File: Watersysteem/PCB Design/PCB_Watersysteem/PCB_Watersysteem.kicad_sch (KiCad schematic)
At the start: 54 parts, among them J1 Screw_Terminal_01x02, J10 LED Water Level, J11 LED Nutrient Level, J12 Height Nutrients, J13 Height Mixer, J2 Conn_01x04_Pin, J21 Voedingstoffen 1, J3 ReferentieProbe, J4 Voedingstoffen 2, J5 Voedingstoffen 3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

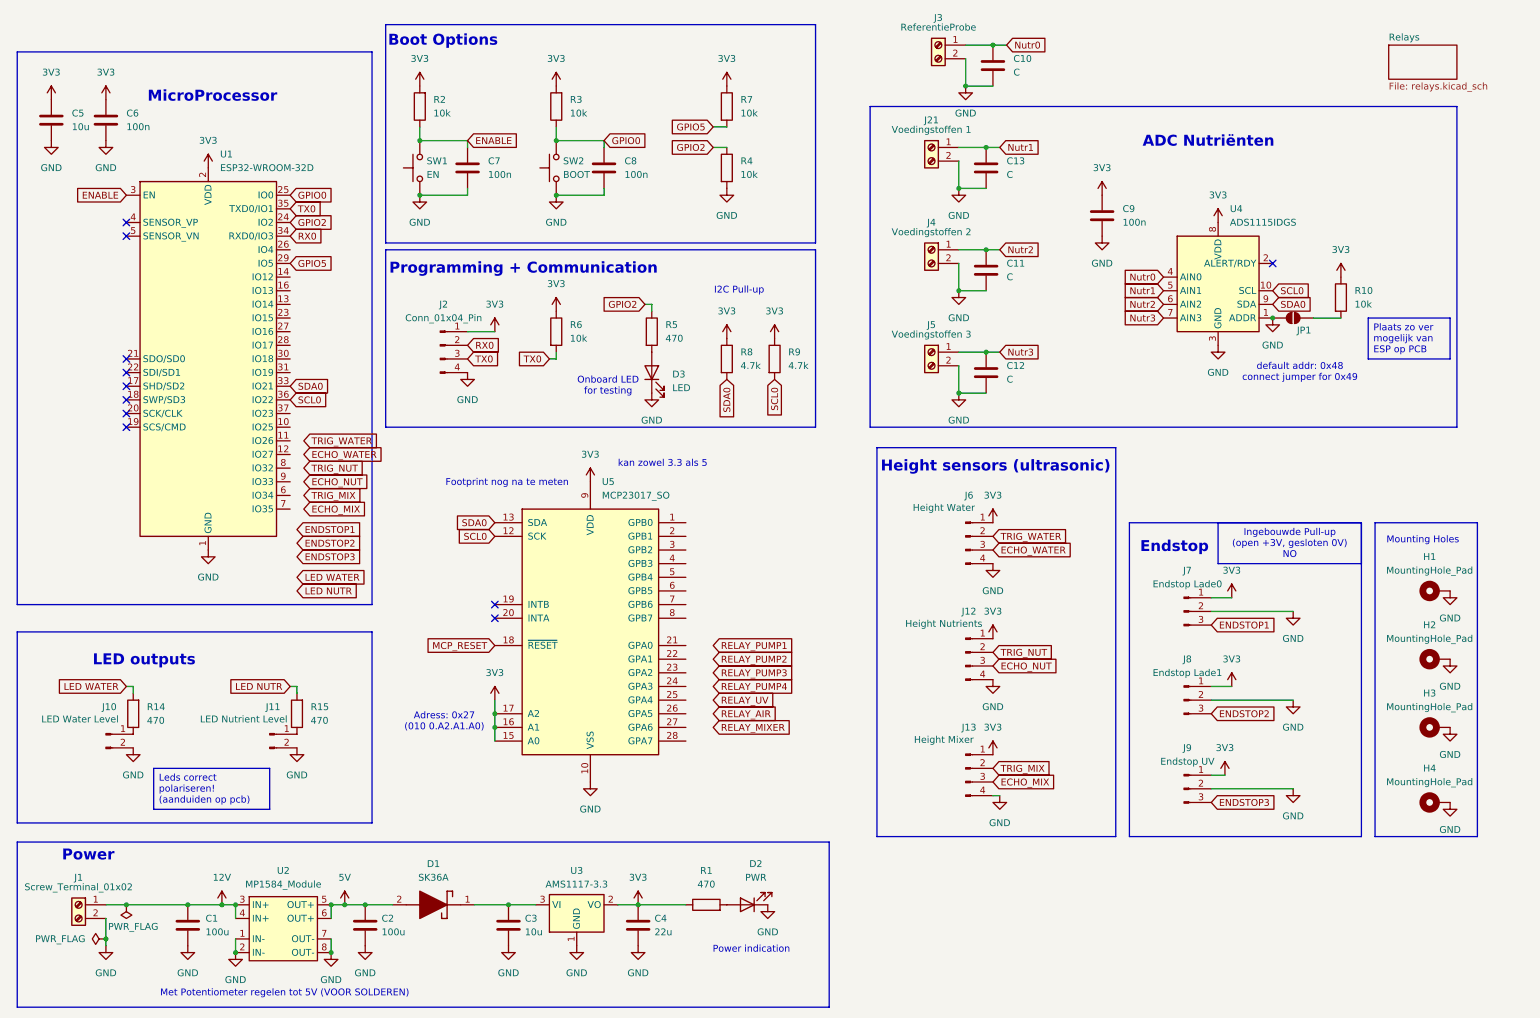
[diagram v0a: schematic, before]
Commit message: PCB update
Testpunten, relaisschakelingen afgewerkt, adres io expander wijzigbaar, enkele footprints
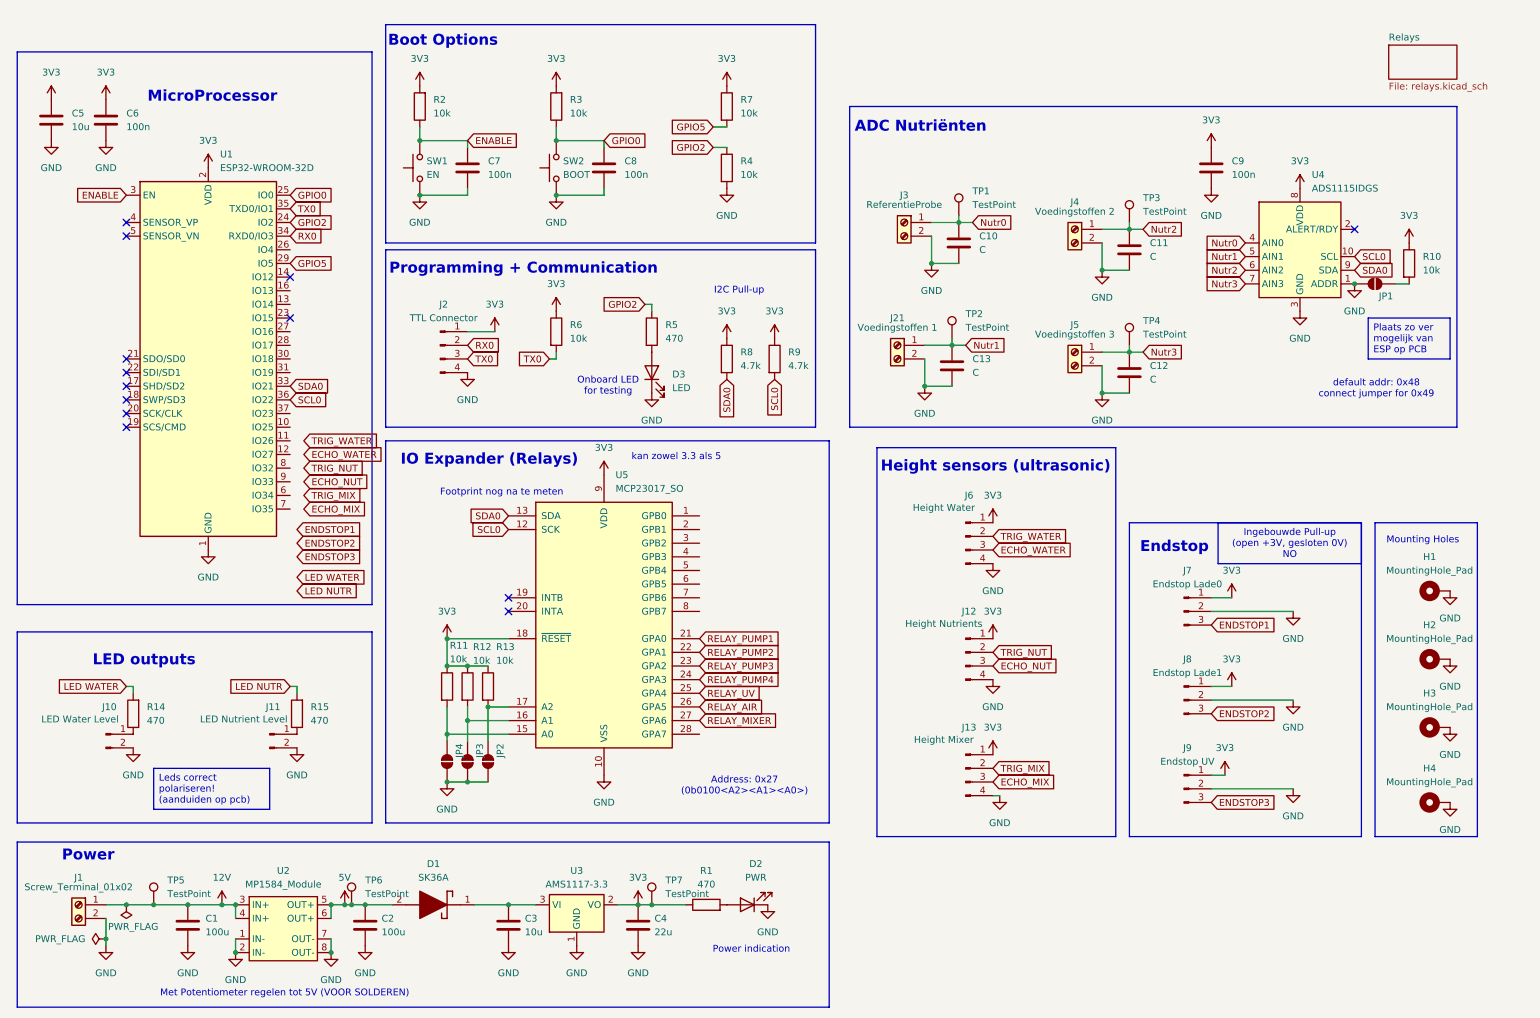
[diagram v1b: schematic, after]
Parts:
- added JP2, JP3, JP4: SolderJumper_2_Open, Jumper:SolderJumper-2_P1.3mm_Open_RoundedPad1.0x1.5mm, symbol Jumper:SolderJumper_2_Open
- added R11, R12, R13: 10k, Resistor_SMD:R_0805_2012Metric_Pad1.20x1.40mm_HandSolder, symbol Device:R
- added TP1, TP2, TP3, TP4, TP5, TP6, TP7: TestPoint, TestPoint:TestPoint_Pad_D2.5mm, symbol Connector:TestPoint
- J10, J11: footprint (none) -> Connector_PinHeader_2.54mm:PinHeader_1x02_P2.54mm_Vertical
- J12, J13, J6: footprint (none) -> Connector_PinHeader_2.54mm:PinHeader_1x04_P2.54mm_Vertical
- J2: value Conn_01x04_Pin -> TTL Connector; footprint (none) -> Connector_PinHeader_2.54mm:PinHeader_1x04_P2.54mm_Vertical
- J7, J8, J9: footprint (none) -> Connector_PinHeader_2.54mm:PinHeader_1x03_P2.54mm_Vertical
- JP1: footprint (none) -> Jumper:SolderJumper-2_P1.3mm_Open_RoundedPad1.0x1.5mm
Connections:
- net MCP_RESET is gone; now on net 3V3: U5.18 (~{RESET})
- net 12V: now also TP5.1
- net 3V3: now also R11.1, R12.1, R13.1, TP7.1; no longer U5.15 (A0), U5.16 (A1), U5.17 (A2)
- net 5V: now also TP6.1
- net GND: now also JP2.1 (A), JP3.1 (A), JP4.1 (A)
- net Nutr0: now also TP1.1
- net Nutr1: now also TP2.1
- net Nutr2: now also TP3.1
- net Nutr3: now also TP4.1
- net RELAY_AIR: now also U5.26 (GPA5)
- net RELAY_MIXER: now also U5.27 (GPA6)
- net RELAY_PUMP1: now also U5.21 (GPA0)
- net RELAY_PUMP2: now also U5.22 (GPA1)
- net RELAY_PUMP3: now also U5.23 (GPA2)
- net RELAY_PUMP4: now also U5.24 (GPA3)
- net RELAY_UV: now also U5.25 (GPA4)
- new net: JP4.2 (B), R11.2, U5.15 (A0)
- new net: JP3.2 (B), R12.2, U5.16 (A1)
- new net: JP2.2 (B), R13.2, U5.17 (A2)
- no-connect marks 11 -> 13
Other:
- note added: "Address: 0x27 (0b0100<A2><A1><A0>)"
- note added: "IO Expander (Relays)"
- note removed: "Adress: 0x27 (010 0.A2.A1.A0)"
- moved on the sheet: C10, C11, C12, C13, C9, J21, J3, J4, J5, JP1, R10, U4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

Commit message: Update PCB
Switch library toegevoegd, IO expander ontkoppel toegevoegd
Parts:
- added C14: 100n, symbol Device:C
- SW1, SW2: footprint (none) -> SamacSys_Parts:Wurth_Tactile_Switch_SPST-NO_434111043826
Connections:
- net 3V3: now also C14.1
- net GND: now also C14.2
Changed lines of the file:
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@@
 			)
 		)
-		(property "Footprint" ""
+		(property "Footprint" "SamacSys_Parts:Wurth_Tactile_Switch_SPST-NO_434111043826"
 			(at 107.95 40.64 0)
 			(effects
@@
 	)
 	(symbol
+		(lib_id "power:VCC")
+		(at 149.86 99.06 0)
+		(unit 1)
+		(exclude_from_sim no)
+		(in_bom yes)
+		(on_board yes)
+		(dnp no)
+		(fields_autoplaced yes)
+		(property "Reference" "#PWR089"
+			(at 149.86 102.87 0)
+			(effects
+				(font
+					(size 1.27 1.27)
+				)
+				(hide yes)
+			)
+		)
+		(property "Value" "3V3"
+			(at 149.86 93.98 0)
+			(effects
+				(font
+					(size 1.27 1.27)
+				)
+			)
+		)
+		(property "Footprint" ""
+			(at 149.86 99.06 0)
+			(effects
+				(font
+					(size 1.27 1.27)
+				)
+				(hide yes)
+			)
+		)
+		(property "Datasheet" ""
+			(at 149.86 99.06 0)
+			(effects
+				(font
+					(size 1.27 1.27)
+				)
+				(hide yes)
+			)
+		)
+		(property "Description" "Power symbol creates a global label with name \"VCC\""
+			(at 149.86 99.06 0)
+			(effects
+				(font
+					(size 1.27 1.27)
+				)
+				(hide yes)
+			)
+		)
+		(pin "1"
+		)
+		(instances
+			(project "PCB_Watersysteem"
+				(path "/de0b8b90-8fde-4ab1-b1b1-e85d44454ecd"
+					(reference "#PWR089")
+					(unit 1)
+				)
+			)
+		)
+	)
+	(symbol
 		(lib_id "Mechanical:MountingHole_Pad")
 		(at 276.86 144.78 90)
@@
 			)
 		)
-		(property "Footprint" ""
+		(property "Footprint" "SamacSys_Parts:Wurth_Tactile_Switch_SPST-NO_434111043826"
 			(at 82.55 40.64 0)
 			(effects
@@
 	(symbol
 		(lib_id "power:GND")
+		(at 149.86 106.68 0)
+		(unit 1)
+		(exclude_from_sim no)
+		(in_bom yes)
+		(on_board yes)
+		(dnp no)
+		(fields_autoplaced yes)
+		(property "Reference" "#PWR088"
+			(at 149.86 113.03 0)
+			(effects
+				(font
+					(size 1.27 1.27)
+				)
+				(hide yes)
+			)
+		)
+		(property "Value" "GND"
+			(at 149.86 111.76 0)
+			(effects
+				(font
+					(size 1.27 1.27)
+				)
+			)
+		)
+		(property "Footprint" ""
+			(at 149.86 106.68 0)
+			(effects
+				(font
+					(size 1.27 1.27)
+				)
+				(hide yes)
+			)
+		)
+		(property "Datasheet" ""
+			(at 149.86 106.68 0)
+			(effects
+				(font
+					(size 1.27 1.27)
+				)
+				(hide yes)
+			)
+		)
+		(property "Description" "Power symbol creates a global label with name \"GND\" , ground"
+			(at 149.86 106.68 0)
+			(effects
+				(font
+					(size 1.27 1.27)
+				)
+				(hide yes)
+			)
+		)
+		(pin "1"
+		)
+		(instances
+			(project "PCB_Watersysteem"
+				(path "/de0b8b90-8fde-4ab1-b1b1-e85d44454ecd"
+					(reference "#PWR088")
+					(unit 1)
+				)
+			)
+		)
+	)
+	(symbol
+		(lib_id "power:GND")
 		(at 92.71 154.94 0)
 		(unit 1)
@@
 					(unit 1)
 				)
+			)
+		)
+	)
+	(symbol
+		(lib_id "Device:C")
+		(at 149.86 102.87 0)
+		(unit 1)
+		(exclude_from_sim no)
+		(in_bom yes)
+		(on_board yes)
+		(dnp no)
+		(fields_autoplaced yes)
+		(property "Reference" "C14"
+			(at 153.67 101.5999 0)
+			(effects
+				(font
+					(size 1.27 1.27)
+				)
+				(justify left)
+			)
+		)
+		(property "Value" "100n"
+			(at 153.67 104.1399 0)
+			(effects
+				(font
+					(size 1.27 1.27)
+				)
+				(justify left)
+			)
+		)
+		(property "Footprint" ""
+			(at 150.8252 106.68 0)
+			(effects
+				(font
+					(size 1.27 1.27)
+				)
+				(hide yes)
+			)
+		)
+		(property "Datasheet" "~"
+			(at 149.86 102.87 0)
+			(effects
+				(font
+					(size 1.27 1.27)
+				)
+				(hide yes)
+			)
+		)
+		(property "Description" "Unpolarized capacitor"
+			(at 149.86 102.87 0)
+			(effects
+				(font
+					(size 1.27 1.27)
+				)
+				(hide yes)
+			)
+		)
+		(pin "2"
+		)
+		(pin "1"
+		)
+		(instances
+			(project ""
+				(path "/de0b8b90-8fde-4ab1-b1b1-e85d44454ecd"
+					(reference "C14")
+					(unit 1)
+				)

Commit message: Update PCB
Footprints toegevoegd
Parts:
- H1, H2, H3, H4: footprint (none) -> MountingHole:MountingHole_4.3mm_M4_DIN965_Pad_TopBottom
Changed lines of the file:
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@@
 			)
 		)
-		(property "Footprint" ""
+		(property "Footprint" "MountingHole:MountingHole_4.3mm_M4_DIN965_Pad_TopBottom"
 			(at 276.86 144.78 0)
 			(effects
@@
 			)
 		)
-		(property "Footprint" ""
+		(property "Footprint" "MountingHole:MountingHole_4.3mm_M4_DIN965_Pad_TopBottom"
 			(at 276.86 158.75 0)
 			(effects
@@
 			)
 		)
-		(property "Footprint" ""
+		(property "Footprint" "MountingHole:MountingHole_4.3mm_M4_DIN965_Pad_TopBottom"
 			(at 276.86 132.08 0)
 			(effects
@@
 			)
 		)
-		(property "Footprint" ""
+		(property "Footprint" "MountingHole:MountingHole_4.3mm_M4_DIN965_Pad_TopBottom"
 			(at 276.86 119.38 0)
 			(effects

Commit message: Update PCB
IO gemapt, Condensator ADC, Schematic geprint
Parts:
- added TP15: TestPoint, TestPoint:TestPoint_Pad_D2.5mm, symbol Connector:TestPoint
- C10, C11, C12, C13: value C -> 100n; footprint (none) -> Capacitor_SMD:C_0805_2012Metric_Pad1.18x1.45mm_HandSolder
- C14: footprint (none) -> Capacitor_SMD:C_0805_2012Metric_Pad1.18x1.45mm_HandSolder
- J1: value Screw_Terminal_01x02 -> 12V ingang
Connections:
- net ECHO_MIX: now also U1.13 (IO14)
- net ECHO_NUT: now also U1.11 (IO26)
- net ECHO_WATER: now also U1.9 (IO33)
- net ENDSTOP1: now also U1.28 (IO17)
- net ENDSTOP2: now also U1.27 (IO16)
- net ENDSTOP3: now also U1.26 (IO4)
- net GND: now also TP15.1
- net LED NUTR: now also U1.31 (IO19)
- net LED WATER: now also U1.30 (IO18)
- net TRIG_MIX: now also U1.12 (IO27)
- net TRIG_NUT: now also U1.10 (IO25)
- net TRIG_WATER: now also U1.8 (IO32)
- no-connect marks 13 -> 26
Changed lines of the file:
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@@
 	)
 	(no_connect
+		(at 139.7 115.57)
+	)
+	(no_connect
 		(at 104.14 123.19)
 	)
@@
 	)
 	(no_connect
+		(at 139.7 113.03)
+	)
+	(no_connect
+		(at 139.7 107.95)
+	)
+	(no_connect
+		(at 139.7 105.41)
+	)
+	(no_connect
+		(at 139.7 146.05)
+	)
+	(no_connect
 		(at 63.5 68.58)
 	)
 	(no_connect
+		(at 139.7 110.49)
+	)
+	(no_connect
 		(at 261.62 52.07)
 	)
 	(no_connect
+		(at 63.5 63.5)
+	)
+	(no_connect
 		(at 33.02 86.36)
 	)
@@
 	)
 	(no_connect
+		(at 63.5 101.6)
+	)
+	(no_connect
+		(at 63.5 104.14)
+	)
+	(no_connect
+		(at 139.7 123.19)
+	)
+	(no_connect
 		(at 104.14 120.65)
 	)
 	(no_connect
+		(at 63.5 86.36)
+	)
+	(no_connect
 		(at 33.02 78.74)
 	)
 	(no_connect
+		(at 139.7 120.65)
+	)
+	(no_connect
 		(at 33.02 50.8)
 	)
 	(no_connect
+		(at 139.7 118.11)
+	)
+	(no_connect
 		(at 33.02 76.2)
 	)
@@
 	(global_label "TRIG_WATER"
 		(shape input)
-		(at 66.04 91.44 0)
+		(at 63.5 96.52 0)
 		(fields_autoplaced yes)
 		(effects
@@
 		)
 		(property "Intersheetrefs" "${INTERSHEET_REFS}"
-			(at 80.0318 91.44 0)
+			(at 77.4918 96.52 0)
 			(effects
 				(font
@@
 	(global_label "ENDSTOP2"
 		(shape input)
-		(at 64.77 110.49 0)
+		(at 63.5 71.12 0)
 		(fields_autoplaced yes)
 		(effects
@@
 		)
 		(property "Intersheetrefs" "${INTERSHEET_REFS}"
-			(at 77.4918 110.49 0)
+			(at 76.2218 71.12 0)
 			(effects
 				(font
@@
 	(global_label "ECHO_MIX"
 		(shape input)
-		(at 66.04 104.14 0)
+		(at 63.5 66.04 0)
 		(fields_autoplaced yes)
 		(effects
@@
 		)
 		(property "Intersheetrefs" "${INTERSHEET_REFS}"
-			(at 78.3385 104.14 0)
+			(at 75.7985 66.04 0)
 			(effects
 				(font
@@
 	(global_label "ENDSTOP1"
 		(shape input)
-		(at 64.77 107.95 0)
+		(at 63.5 73.66 0)
 		(fields_autoplaced yes)
 		(effects
@@
 		)
 		(property "Intersheetrefs" "${INTERSHEET_REFS}"
-			(at 77.4918 107.95 0)
+			(at 76.2218 73.66 0)
 			(effects
 				(font
@@
 	(global_label "TRIG_NUT"
 		(shape input)
-		(at 66.04 96.52 0)
+		(at 63.5 88.9 0)
 		(fields_autoplaced yes)
 		(effects
@@
 		)
 		(property "Intersheetrefs" "${INTERSHEET_REFS}"
-			(at 77.7338 96.52 0)
+			(at 75.1938 88.9 0)
 			(effects
 				(font
@@
 	(global_label "LED NUTR"
 		(shape input)
-		(at 64.77 119.38 0)
+		(at 63.5 78.74 0)
 		(fields_autoplaced yes)
 		(effects
@@
 		)
 		(property "Intersheetrefs" "${INTERSHEET_REFS}"
-			(at 77.0685 119.38 0)
+			(at 75.7985 78.74 0)
 			(effects
 				(font
@@
 	(global_label "ECHO_NUT"
 		(shape input)
-		(at 66.04 99.06 0)
+		(at 63.5 91.44 0)
 		(fields_autoplaced yes)
 		(effects
@@
 		)
 		(property "Intersheetrefs" "${INTERSHEET_REFS}"
-			(at 78.7014 99.06 0)
+			(at 76.1614 91.44 0)
 			(effects
 				(font
@@
 	(global_label "TRIG_MIX"
 		(shape input)
-		(at 66.04 101.6 0)
+		(at 63.5 93.98 0)
 		(fields_autoplaced yes)
 		(effects
@@
 		)
 		(property "Intersheetrefs" "${INTERSHEET_REFS}"
-			(at 77.3709 101.6 0)
+			(at 74.8309 93.98 0)
 			(effects
 				(font
@@
 	(global_label "ENDSTOP3"
 		(shape input)
-		(at 64.77 113.03 0)
+		(at 63.5 55.88 0)
 		(fields_autoplaced yes)
 		(effects
@@
 		)
 		(property "Intersheetrefs" "${INTERSHEET_REFS}"
-			(at 77.4918 113.03 0)
+			(at 76.2218 55.88 0)
 			(effects
 				(font
@@
 	(global_label "ECHO_WATER"
 		(shape input)
-		(at 66.04 93.98 0)
+		(at 63.5 99.06 0)
 		(fields_autoplaced yes)
 		(effects
@@
 		)
 		(property "Intersheetrefs" "${INTERSHEET_REFS}"
-			(at 80.9994 93.98 0)
+			(at 78.4594 99.06 0)
 			(effects
 				(font
@@
 	(global_label "LED WATER"
 		(shape input)
-		(at 64.77 116.84 0)
+		(at 63.5 76.2 0)
 		(fields_autoplaced yes)
 		(effects
@@
 		)
 		(property "Intersheetrefs" "${INTERSHEET_REFS}"
-			(at 78.0965 116.84 0)
+			(at 76.8265 76.2 0)
 			(effects
 				(font
@@
 	)
 	(symbol
+		(lib_id "Connector:TestPoint")
+		(at 29.21 184.15 270)
+		(unit 1)
+		(exclude_from_sim no)
+		(in_bom yes)
+		(on_board yes)
+		(dnp no)
+		(fields_autoplaced yes)
+		(property "Reference" "TP15"
+			(at 34.29 182.8799 90)
+			(effects
+				(font
+					(size 1.27 1.27)
+				)
+				(justify left)
+			)
+		)
+		(property "Value" "TestPoint"
+			(at 34.29 185.4199 90)
+			(effects
+				(font
+					(size 1.27 1.27)
+				)
+				(justify left)
+			)
+		)
+		(property "Footprint" "TestPoint:TestPoint_Pad_D2.5mm"
+			(at 29.21 189.23 0)
+			(effects
+				(font
+					(size 1.27 1.27)
+				)
+				(hide yes)
+			)
+		)
+		(property "Datasheet" "~"
+			(at 29.21 189.23 0)
+			(effects
+				(font
+					(size 1.27 1.27)
+				)
+				(hide yes)
+			)
+		)
+		(property "Description" "test point"
+			(at 29.21 184.15 0)
+			(effects
+				(font
+					(size 1.27 1.27)
+				)
+				(hide yes)
+			)
+		)
+		(pin "1"
+		)
+		(instances
+			(project "PCB_Watersysteem"
+				(path "/de0b8b90-8fde-4ab1-b1b1-e85d44454ecd"
+					(reference "TP15")
+					(unit 1)
+				)
+			)
+		)
+	)
+	(symbol
 		(lib_id "Device:R")
 		(at 113.03 29.21 180)
@@
 			)
 		)
-		(property "Value" "C"
+		(property "Value" "100n"
 			(at 190.5 78.7399 0)
 			(effects
@@
 			)
 		)
-		(property "Footprint" ""
+		(property "Footprint" "Capacitor_SMD:C_0805_2012Metric_Pad1.18x1.45mm_HandSolder"
 			(at 187.6552 81.28 0)
 			(effects
@@
 	(symbol
 		(lib_id "power:PWR_FLAG")
-		(at 33.02 177.8 180)
+		(at 33.02 177.8 0)
 		(unit 1)
 		(exclude_from_sim no)
@@
 		(dnp no)
 		(property "Reference" "#FLG02"
-			(at 33.02 179.705 0)
+			(at 33.02 175.895 0)
 			(effects
 				(font
@@
 		)
 		(property "Value" "PWR_FLAG"
-			(at 34.29 181.864 0)
+			(at 31.75 173.736 0)
 			(effects
 				(font
@@
 			)
 		)
-		(property "Value" "C"
+		(property "Value" "100n"
 			(at 223.52 57.1499 0)
 			(effects
@@
 			)
 		)
-		(property "Footprint" ""
+		(property "Footprint" "Capacitor_SMD:C_0805_2012Metric_Pad1.18x1.45mm_HandSolder"
 			(at 220.6752 59.69 0)
 			(effects
@@
 			)
 		)
-		(property "Value" "C"
+		(property "Value" "100n"
 			(at 223.52 80.0099 0)
 			(effects
@@
 			)
 		)
-		(property "Footprint" ""
+		(property "Footprint" "Capacitor_SMD:C_0805_2012Metric_Pad1.18x1.45mm_HandSolder"
 			(at 220.6752 82.55 0)
 			(effects
@@
 			)
 		)
-		(property "Value" "C"
+		(property "Value" "100n"
 			(at 191.77 55.8799 0)
 			(effects
@@
 			)
 		)
-		(property "Footprint" ""
+		(property "Footprint" "Capacitor_SMD:C_0805_2012Metric_Pad1.18x1.45mm_HandSolder"
 			(at 188.9252 58.42 0)
 			(effects
@@
 			)
 		)
-		(property "Footprint" ""
+		(property "Footprint" "Capacitor_SMD:C_0805_2012Metric_Pad1.18x1.45mm_HandSolder"
 			(at 150.8252 106.68 0)
 			(effects
@@
 			)
 		)
-		(property "Value" "Screw_Terminal_01x02"
-			(at 24.13 174.498 0)
+		(property "Value" "12V ingang"
+			(at 20.828 174.498 0)
 			(effects
 				(font
